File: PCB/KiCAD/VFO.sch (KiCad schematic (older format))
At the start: 22 parts, among them CON1 AVR-ISP-6, J1 USB_OTG, U10 LD1117S33TR, U2 ATMEGA8-16AU, U3 ADuM1201CR, U6 FT232RL, U7 SI5351, Y7 8Mhz, Y8 27Mhz

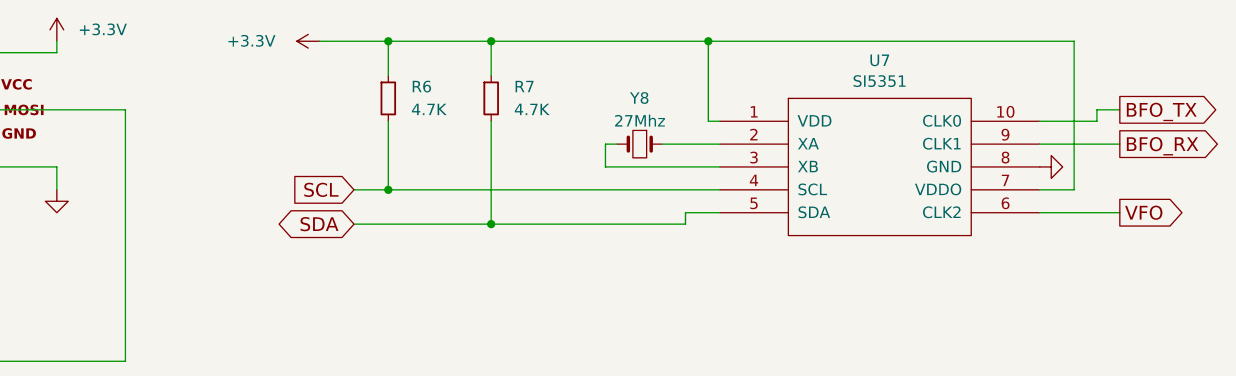
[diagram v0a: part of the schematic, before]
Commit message: delete unused components in DragonFly.lib, move KiCAD project to PCB folder
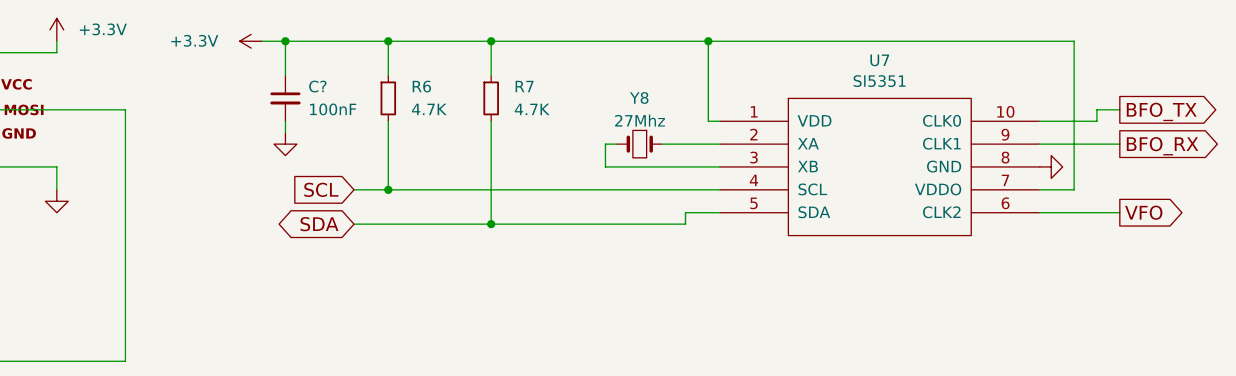
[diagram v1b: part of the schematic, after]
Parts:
- added C?: 100nF, Capacitors_SMD:C_0603_HandSoldering, symbol C_Small
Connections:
- net +3V3: now also C?.1
- net GND: now also C?.2
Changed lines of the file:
@@
 LIBS:contrib
 LIBS:valves
-LIBS:LCSDR
-LIBS:switch_dpst
 LIBS:ftdi
-LIBS:1_9
-LIBS:bfg135
+LIBS:DragonFly
 LIBS:DragonFly-cache
 EELAYER 25 0
@@
 L +3.3V #PWR41
 U 1 1 58A03CC8
-P 7250 700
-F 0 "#PWR41" H 7250 550 50  0001 C CNN
-F 1 "+3.3V" V 7250 1000 50  0000 C CNN
-F 2 "" H 7250 700 50  0000 C CNN
-F 3 "" H 7250 700 50  0000 C CNN
-	1    7250 700
+P 7000 700
+F 0 "#PWR41" H 7000 550 50  0001 C CNN
+F 1 "+3.3V" V 7000 1000 50  0000 C CNN
+F 2 "" H 7000 700 50  0000 C CNN
+F 3 "" H 7000 700 50  0000 C CNN
+	1    7000 700
 	0    -1   -1   0
 $EndComp
@@
 	8950 1050 8950 700
 Wire Wire Line
-	7250 700  10550 700
+	7000 700  10550 700
 Wire Wire Line
 	10550 700  10550 1350
@@
 Wire Wire Line
 	4400 2600 3650 2600
+$Comp
+L C_Small C?
+U 1 1 61063DA5
+P 7100 950
+F 0 "C?" H 7200 1000 50  0000 L CNN
+F 1 "100nF" H 7200 900 50  0000 L CNN
+F 2 "Capacitors_SMD:C_0603_HandSoldering" H 7100 950 50  0001 C CNN
+F 3 "" H 7100 950 50  0000 C CNN
+	1    7100 950
+	1    0    0    -1
+$EndComp
+$Comp
+L GND #PWR?
+U 1 1 61063FC6
+P 7100 1100
+F 0 "#PWR?" H 7100 850 50  0001 C CNN
+F 1 "GND" H 7100 950 50  0001 C CNN
+F 2 "" H 7100 1100 50  0000 C CNN
+F 3 "" H 7100 1100 50  0000 C CNN
+	1    7100 1100
+	1    0    0    -1
+$EndComp
+Wire Wire Line
+	7100 1100 7100 1050
+Wire Wire Line
+	7100 850  7100 700
+Connection ~ 7100 700
 $EndSCHEMATC

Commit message: PCB home
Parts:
- gave numbers to parts that had none: 1
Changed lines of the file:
@@
 EESchema Schematic File Version 2
 LIBS:DragonFly-rescue
-LIBS:bee-rescue
 LIBS:power
 LIBS:device
@@
 $EndComp
 $Comp
-L GND #PWR39
+L GND #PWR46
 U 1 1 589EB3CB
 P 6100 1350
-F 0 "#PWR39" H 6100 1100 50  0001 C CNN
+F 0 "#PWR46" H 6100 1100 50  0001 C CNN
 F 1 "GND" H 6100 1200 50  0001 C CNN
 F 2 "" H 6100 1350 50  0000 C CNN
@@
 $EndComp
 $Comp
-L GND #PWR24
+L GND #PWR31
 U 1 1 589EFCBC
 P 750 2350
-F 0 "#PWR24" H 750 2100 50  0001 C CNN
+F 0 "#PWR31" H 750 2100 50  0001 C CNN
 F 1 "GND" H 750 2200 50  0001 C CNN
 F 2 "" H 750 2350 50  0000 C CNN
@@
 $EndComp
 $Comp
-L GND #PWR25
+L GND #PWR32
 U 1 1 589EFDB6
 P 750 2800
-F 0 "#PWR25" H 750 2550 50  0001 C CNN
+F 0 "#PWR32" H 750 2550 50  0001 C CNN
 F 1 "GND" H 750 2650 50  0001 C CNN
 F 2 "" H 750 2800 50  0000 C CNN
@@
 $EndComp
 $Comp
-L +3.3V #PWR41
+L +3.3V #PWR47
 U 1 1 58A03CC8
 P 7000 700
-F 0 "#PWR41" H 7000 550 50  0001 C CNN
+F 0 "#PWR47" H 7000 550 50  0001 C CNN
 F 1 "+3.3V" V 7000 1000 50  0000 C CNN
 F 2 "" H 7000 700 50  0000 C CNN
@@
 $EndComp
 $Comp
-L GND #PWR31
+L GND #PWR38
 U 1 1 58A061EE
 P 2850 6550
-F 0 "#PWR31" H 2850 6300 50  0001 C CNN
+F 0 "#PWR38" H 2850 6300 50  0001 C CNN
 F 1 "GND" H 2850 6400 50  0001 C CNN
 F 2 "" H 2850 6550 50  0000 C CNN
@@
 $EndComp
 $Comp
-L GND #PWR32
+L GND #PWR39
 U 1 1 58A09E30
 P 3400 6900
-F 0 "#PWR32" H 3400 6650 50  0001 C CNN
+F 0 "#PWR39" H 3400 6650 50  0001 C CNN
 F 1 "GND" H 3400 6750 50  0001 C CNN
 F 2 "" H 3400 6900 50  0000 C CNN
@@
 $EndComp
 $Comp
-L GND #PWR33
+L GND #PWR40
 U 1 1 58A0C9D9
 P 4150 6900
-F 0 "#PWR33" H 4150 6650 50  0001 C CNN
+F 0 "#PWR40" H 4150 6650 50  0001 C CNN
 F 1 "GND" H 4150 6750 50  0001 C CNN
 F 2 "" H 4150 6900 50  0000 C CNN
@@
 BFO_TX
 $Comp
-L GND #PWR48
+L GND #PWR56
 U 1 1 58E0B7EA
 P 10400 1250
-F 0 "#PWR48" H 10400 1000 50  0001 C CNN
+F 0 "#PWR56" H 10400 1000 50  0001 C CNN
 F 1 "GND" H 10400 1100 50  0001 C CNN
 F 2 "" H 10400 1250 50  0000 C CNN
@@
 SCL
 $Comp
-L +3.3V #PWR38
+L +3.3V #PWR45
 U 1 1 60FBBB98
 P 6100 700
-F 0 "#PWR38" H 6100 550 50  0001 C CNN
+F 0 "#PWR45" H 6100 550 50  0001 C CNN
 F 1 "+3.3V" H 6300 750 50  0000 C CNN
 F 2 "" H 6100 700 50  0000 C CNN
@@
 $EndComp
 $Comp
-L GND #PWR35
+L GND #PWR42
 U 1 1 60FBEFE8
 P 4550 4450
-F 0 "#PWR35" H 4550 4200 50  0001 C CNN
+F 0 "#PWR42" H 4550 4200 50  0001 C CNN
 F 1 "GND" H 4550 4300 50  0001 C CNN
 F 2 "" H 4550 4450 50  0000 C CNN
@@
 $EndComp
 $Comp
-L +3.3V #PWR34
+L +3.3V #PWR41
 U 1 1 60FBF348
 P 4550 3950
-F 0 "#PWR34" H 4550 3800 50  0001 C CNN
+F 0 "#PWR41" H 4550 3800 50  0001 C CNN
 F 1 "+3.3V" V 4550 4200 50  0000 C CNN
 F 2 "" H 4550 3950 50  0000 C CNN
@@
 $EndComp
 $Comp
-L GNDD #PWR44
+L GNDD #PWR52
 U 1 1 60FC3E83
 P 8650 4700
-F 0 "#PWR44" H 8650 4450 50  0001 C CNN
+F 0 "#PWR52" H 8650 4450 50  0001 C CNN
 F 1 "GNDD" H 8650 4575 50  0001 C CNN
 F 2 "" H 8650 4700 50  0001 C CNN
@@
 $EndComp
 $Comp
-L GNDD #PWR43
+L GNDD #PWR51
 U 1 1 60FC3F82
 P 8650 4000
-F 0 "#PWR43" H 8650 3750 50  0001 C CNN
+F 0 "#PWR51" H 8650 3750 50  0001 C CNN
 F 1 "GNDD" H 8650 3875 50  0001 C CNN
 F 2 "" H 8650 4000 50  0001 C CNN
@@
 $EndComp
 $Comp
-L GNDD #PWR47
+L GNDD #PWR55
 U 1 1 60FC3FE1
 P 10250 4750
-F 0 "#PWR47" H 10250 4500 50  0001 C CNN
+F 0 "#PWR55" H 10250 4500 50  0001 C CNN
 F 1 "GNDD" H 10250 4625 50  0001 C CNN
 F 2 "" H 10250 4750 50  0001 C CNN
@@
 $EndComp
 $Comp
-L GNDD #PWR37
+L GNDD #PWR44
 U 1 1 60FC45C5
 P 5650 4450
-F 0 "#PWR37" H 5650 4200 50  0001 C CNN
+F 0 "#PWR44" H 5650 4200 50  0001 C CNN
 F 1 "GNDD" H 5650 4325 50  0001 C CNN
 F 2 "" H 5650 4450 50  0001 C CNN
@@
 $EndComp
 $Comp
-L GNDD #PWR40
+L GNDD #PWR48
 U 1 1 60FC465C
 P 7000 5900
-F 0 "#PWR40" H 7000 5650 50  0001 C CNN
+F 0 "#PWR48" H 7000 5650 50  0001 C CNN
 F 1 "GNDD" H 7000 5775 50  0001 C CNN
 F 2 "" H 7000 5900 50  0001 C CNN
@@
 $EndComp
 $Comp
-L GNDD #PWR45
+L GNDD #PWR53
 U 1 1 60FC82A8
 P 8700 3600
-F 0 "#PWR45" H 8700 3350 50  0001 C CNN
+F 0 "#PWR53" H 8700 3350 50  0001 C CNN
 F 1 "GNDD" H 8700 3475 50  0001 C CNN
 F 2 "" H 8700 3600 50  0001 C CNN
@@
 $EndComp
 $Comp
-L GNDD #PWR46
+L GNDD #PWR54
 U 1 1 60FC8353
 P 9650 3600
-F 0 "#PWR46" H 9650 3350 50  0001 C CNN
+F 0 "#PWR54" H 9650 3350 50  0001 C CNN
 F 1 "GNDD" H 9650 3475 50  0001 C CNN
 F 2 "" H 9650 3600 50  0001 C CNN
@@
 $EndComp
 $Comp
-L GNDD #PWR42
+L GNDD #PWR50
 U 1 1 60FC83BE
 P 7600 3550
-F 0 "#PWR42" H 7600 3300 50  0001 C CNN
+F 0 "#PWR50" H 7600 3300 50  0001 C CNN
 F 1 "GNDD" H 7600 3425 50  0001 C CNN
 F 2 "" H 7600 3550 50  0001 C CNN
@@
 $EndComp
 $Comp
-L +3.3V #PWR30
+L +3.3V #PWR37
 U 1 1 60FCB4EA
 P 2650 1250
-F 0 "#PWR30" H 2650 1100 50  0001 C CNN
+F 0 "#PWR37" H 2650 1100 50  0001 C CNN
 F 1 "+3.3V" H 2850 1300 50  0000 C CNN
 F 2 "" H 2650 1250 50  0000 C CNN
@@
 	4950 1450 1600 1450
 $Comp
-L GND #PWR29
+L GND #PWR36
 U 1 1 60FCC081
 P 2600 4550
-F 0 "#PWR29" H 2600 4300 50  0001 C CNN
+F 0 "#PWR36" H 2600 4300 50  0001 C CNN
 F 1 "GND" H 2600 4400 50  0001 C CNN
 F 2 "" H 2600 4550 50  0000 C CNN
@@
 Connection ~ 2600 4500
 $Comp
-L +3.3V #PWR36
+L +3.3V #PWR43
 U 1 1 60FCC6C5
 P 4700 6250
-F 0 "#PWR36" H 4700 6100 50  0001 C CNN
+F 0 "#PWR43" H 4700 6100 50  0001 C CNN
 F 1 "+3.3V" V 4700 6500 50  0000 C CNN
 F 2 "" H 4700 6250 50  0000 C CNN
@@
 $EndComp
 $Comp
-L +12V #PWR28
+L +12V #PWR35
 U 1 1 60FCCDC8
 P 2300 6150
-F 0 "#PWR28" H 2300 6000 50  0001 C CNN
+F 0 "#PWR35" H 2300 6000 50  0001 C CNN
 F 1 "+12V" H 2300 6290 50  0000 C CNN
 F 2 "" H 2300 6150 50  0000 C CNN
@@
 TX_TRX
 $Comp
-L GND #PWR27
+L GND #PWR34
 U 1 1 60FE3270
 P 1650 2200
-F 0 "#PWR27" H 1650 1950 50  0001 C CNN
+F 0 "#PWR34" H 1650 1950 50  0001 C CNN
 F 1 "GND" H 1650 2050 50  0001 C CNN
 F 2 "" H 1650 2200 50  0000 C CNN
@@
 $EndComp
 $Comp
-L GND #PWR26
+L GND #PWR33
 U 1 1 610504BE
 P 1150 2100
-F 0 "#PWR26" H 1150 1850 50  0001 C CNN
+F 0 "#PWR33" H 1150 1850 50  0001 C CNN
 F 1 "GND" H 1150 1950 50  0001 C CNN
 F 2 "" H 1150 2100 50  0000 C CNN
@@
 	4400 2600 3650 2600
 $Comp
-L C_Small C?
+L C_Small C43
 U 1 1 61063DA5
 P 7100 950
-F 0 "C?" H 7200 1000 50  0000 L CNN
+F 0 "C43" H 7200 1000 50  0000 L CNN
 F 1 "100nF" H 7200 900 50  0000 L CNN
 F 2 "Capacitors_SMD:C_0603_HandSoldering" H 7100 950 50  0001 C CNN
@@
 $EndComp
 $Comp
-L GND #PWR?
+L GND #PWR49
 U 1 1 61063FC6
 P 7100 1100
-F 0 "#PWR?" H 7100 850 50  0001 C CNN
+F 0 "#PWR49" H 7100 850 50  0001 C CNN
 F 1 "GND" H 7100 950 50  0001 C CNN
 F 2 "" H 7100 1100 50  0000 C CNN
